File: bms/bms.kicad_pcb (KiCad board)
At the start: 2 copper layers, 89.7 x 150.1 mm, 27 parts, among them J1 Conn_01x16_Pin, J10 Conn_01x02_Pin, J11 Conn_01x02_Pin, J12 Conn_01x02_Pin, J13 Conn_01x02_Pin, J14 Conn_01x08_Pin, J15 Conn_01x08_Pin, J16 Conn_01x02_Pin, J17 Conn_01x08_Pin, J18 Conn_01x08_Pin, J19 Conn_01x08_Pin, J2 Conn_01x16_Pin, J20 Conn_01x08_Pin, J21 Conn_01x08_Pin, J22 Conn_01x08_Socket, J23 Conn_01x10_Socket, J24 Conn_01x08_Pin, J25 Conn_01x02_Pin, J26 Conn_01x06_Socket, J27 Conn_01x06_Socket, J3 Conn_01x02_Pin, J4 Conn_01x02_Pin, J5 Conn_01x02_Pin, J6 Conn_01x16_Pin, J7 Conn_01x20_Pin, J8 Conn_01x20_Pin, J9 Conn_01x02_Pin

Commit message: prajeala_maxima_3
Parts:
- removed the J1 at (114.6, 74.7)
- removed the J2 at (114.6, 51.8)
- removed the J6 at (162.8, 87.4)
- removed the J7 at (114.6, 97.5)
- removed the J8 at (162.8, 115.3)
- added J10: Conn_02x08_Odd_Even, Connector_PinHeader_2.54mm:PinHeader_2x08_P2.54mm_Vertical, B.Cu at (279.6, 123.8)
- added J11: Conn_02x10_Odd_Even, Connector_PinHeader_2.54mm:PinHeader_2x10_P2.54mm_Vertical, B.Cu at (279.7, 151.7)
- added J20: Conn_02x08_Odd_Even, Connector_PinHeader_2.54mm:PinHeader_2x08_P2.54mm_Vertical, B.Cu at (231.4, 88.2)
- added J21: Conn_02x08_Odd_Even, Connector_PinHeader_2.54mm:PinHeader_2x08_P2.54mm_Vertical, B.Cu at (231.4, 111.1)
- added J22: Conn_02x10_Odd_Even, Connector_PinHeader_2.54mm:PinHeader_2x10_P2.54mm_Vertical, B.Cu at (231.4, 133.9)
- moved J7 98.1 mm to (220.6, 43.6)
- moved J12 98.1 mm to (245.6, 43.6)
- moved J13 98.1 mm to (253.9, 43.6)
- moved J23 98.1 mm to (262.3, 43.6)
- moved J8 98.1 mm to (228.9, 43.6)
- moved J9 98.1 mm to (237.2, 43.6)
- moved J4 98.1 mm to (212.2, 43.6)
- moved J1 98.1 mm to (270.6, 43.6)
- moved J25 65.0 mm to (50.8, 148.8)
- moved J24 65.0 mm to (50.8, 157.9)
- moved J2 64.7 mm to (155.0, 109.3)
- moved J3 64.7 mm to (155.0, 132.1)
- moved J5 64.7 mm to (202.9, 105.5)
- moved J6 64.7 mm to (202.9, 132.1)
- moved J27 63.8 mm to (87.3, 153.0)
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- renumbered J24 to J1, J19 to J12, J20 to J13, J11 to J14, J13 to J15, J4 to J17, J9 to J18, J10 to J19, J22 to J2, J21 to J23, J3 to J24, J5 to J25, J25 to J26, J12 to J27, J27 to J3, J14 to J4, J23 to J5, J26 to J6, J15 to J7, J17 to J8, J18 to J9
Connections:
- J26 pad 1: Net-(J23-Pin_10) -> GND
- J26 pad 2: Net-(J2-Pin_16) -> Vout+
- J5 pad 10: Net-(J23-Pin_10) -> unconnected-(J5-Pin_10-Pad10)
- J5 pad 2: unconnected-(J23-Pin_2-Pad2) -> cs
- J5 pad 3: unconnected-(J23-Pin_3-Pad3) -> sout
- J5 pad 4: cs -> miso
- J5 pad 5: sout -> sck
- J5 pad 6: miso -> Vdd
- J5 pad 7: sck -> unconnected-(J5-Pin_7-Pad7)
- J5 pad 8: Vdd -> GND
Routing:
- net Net-(J2-Pin_16): track 93.8 -> 0.00 mm
- net sout: track 83.3 -> 0.00 mm
- net Net-(J16-Pin_2): track 74.9 -> 0.00 mm
- net Vdd: track 72.2 -> 0.00 mm
- net 8: track 129.7 -> 58.4 mm
- net Net-(J15-Pin_2): track 69.8 -> 0.00 mm
- net Net-(J15-Pin_1): track 69.7 -> 0.00 mm
- net Net-(J16-Pin_1): track 69.2 -> 0.00 mm
- net Net-(J23-Pin_10): track 68.0 -> 0.00 mm
- net Net-(J14-Pin_1): track 65.6 -> 0.00 mm
- net 7: track 123.5 -> 58.4 mm
- net Net-(J14-Pin_2): track 64.5 -> 0.00 mm
- net 6: track 118.2 -> 58.4 mm
- net Net-(J17-Pin_2): track 56.6 -> 0.00 mm
- net 5: track 112.8 -> 58.4 mm
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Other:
- board outline removed

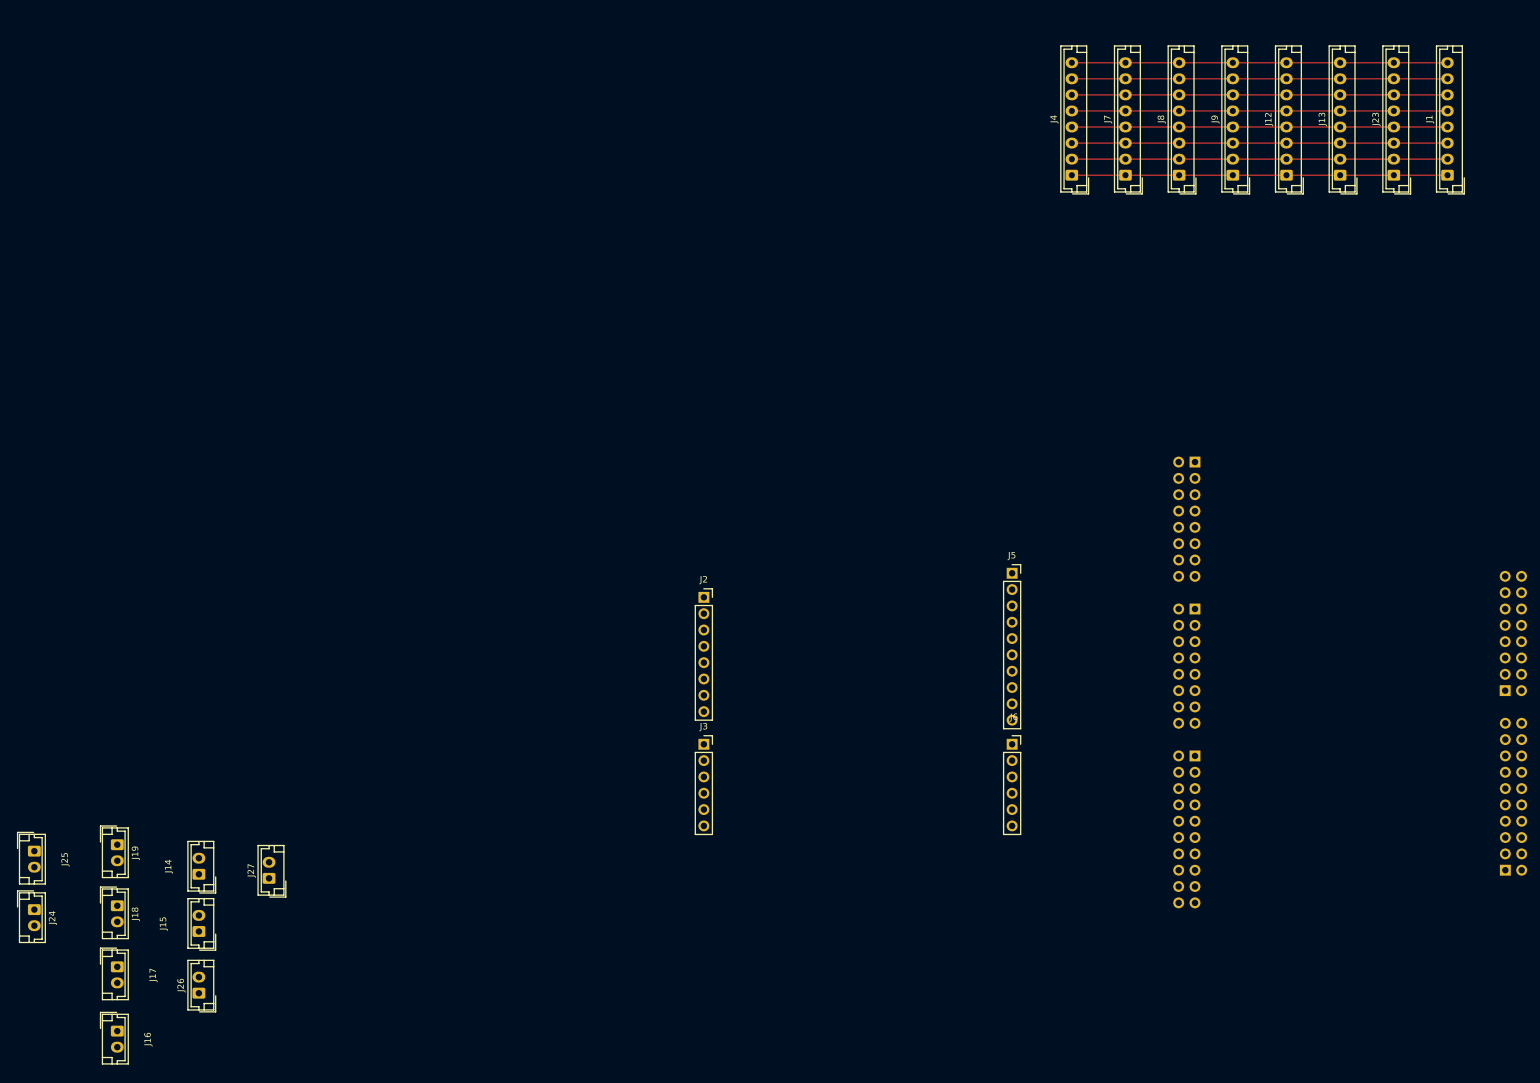
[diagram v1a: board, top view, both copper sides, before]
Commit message: idee de pcb bms
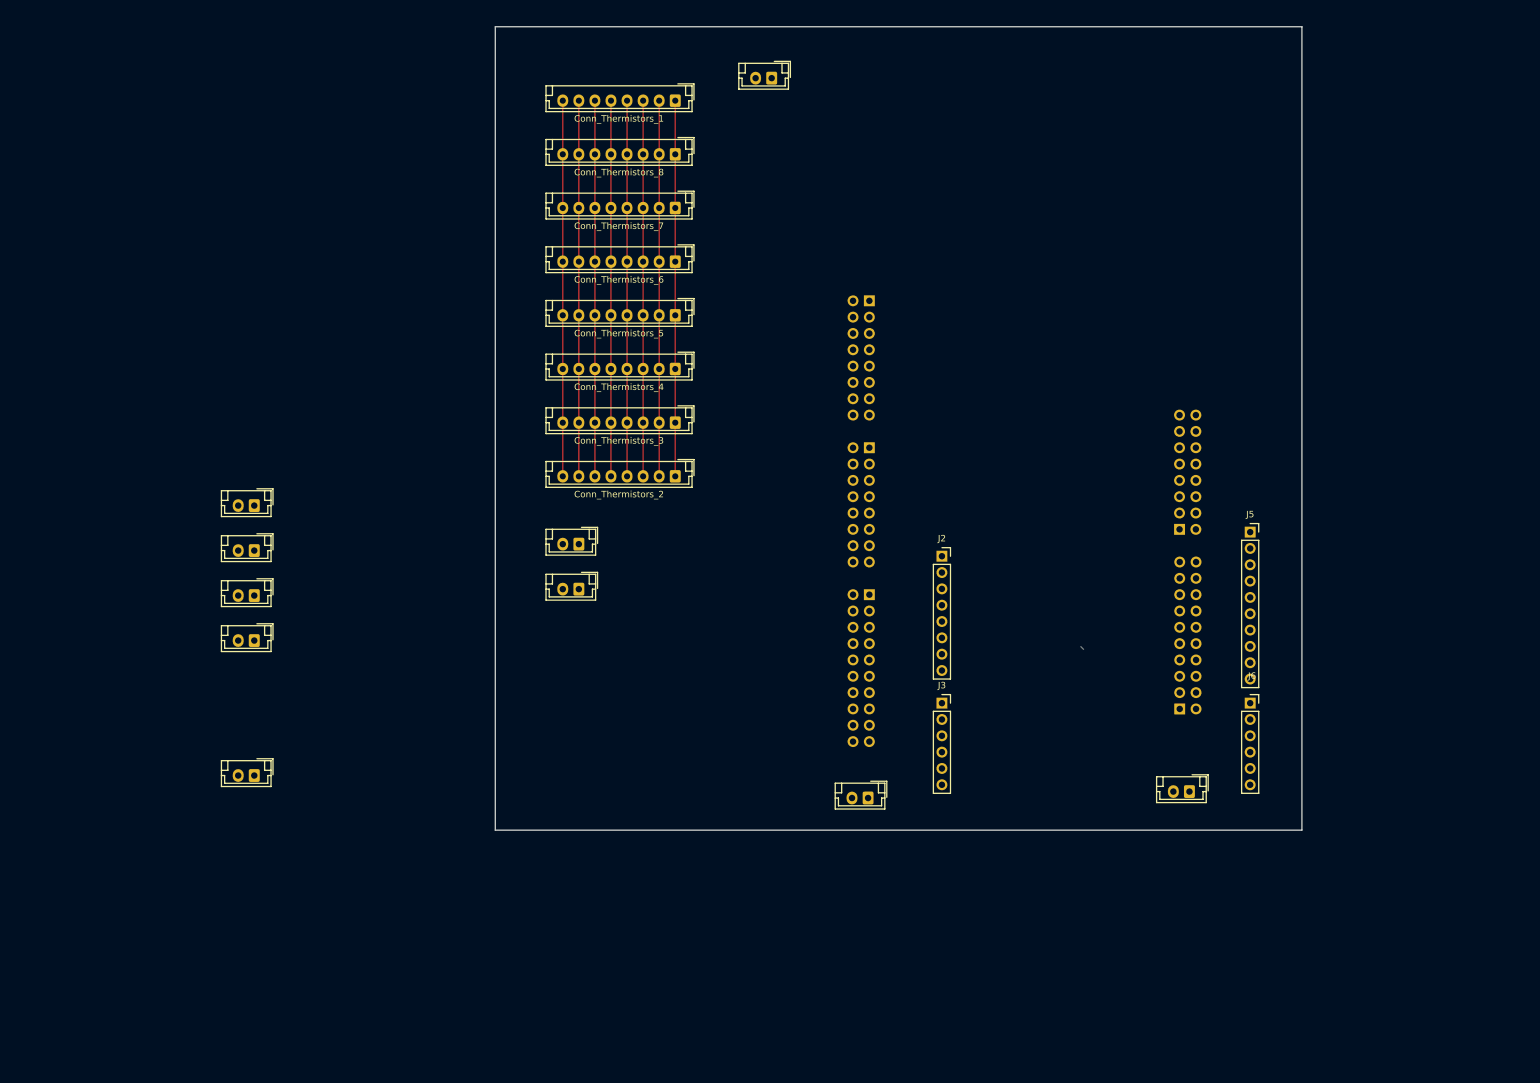
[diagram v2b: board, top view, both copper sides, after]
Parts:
- moved Soft_G_B5-6 179.9 mm to (165.5, 28.5), turned to 180 degrees
- moved Vdd1 143.8 mm to (230.5, 139.5), turned to 180 degrees
- moved Conn_Thermistors_1 120.7 mm to (150.5, 32.0), turned to 180 degrees
- moved Conn_Thermistors_8 111.8 mm to (150.5, 40.4), turned to 180 degrees
- moved Battery1 108.5 mm to (180.5, 140.5), turned to 180 degrees
- moved Conn_Thermistors_7 103.6 mm to (150.5, 48.7), turned to 180 degrees
- moved Conn_Thermistors_6 96.0 mm to (150.5, 57.0), turned to 180 degrees
- moved Conn_Thermistors_5 89.4 mm to (150.5, 65.4), turned to 180 degrees
- moved Soft_G_B1-2 84.4 mm to (135.5, 101.0), turned to 180 degrees
- moved Conn_Thermistors_4 84.0 mm to (150.5, 73.8), turned to 180 degrees
- moved Conn_Thermistors_3 79.9 mm to (150.5, 82.1), turned to 180 degrees
- moved Conn_Thermistors_2 77.5 mm to (150.5, 90.5), turned to 180 degrees
- moved Soft_G_B3-4 73.9 mm to (135.5, 108.0), turned to 180 degrees
- moved Soft_G_B15-16 68.2 mm to (85.0, 102.0), turned to 180 degrees
- moved Soft_G_B7-8 63.7 mm to (85.0, 95.0), turned to 180 degrees
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- renumbered J26 to Battery1, J1 to Conn_Thermistors_1, J4 to Conn_Thermistors_2, J7 to Conn_Thermistors_3, J8 to Conn_Thermistors_4, J9 to Conn_Thermistors_5, J12 to Conn_Thermistors_6, J13 to Conn_Thermistors_7, J23 to Conn_Thermistors_8, J20 to J13, J21 to J14, J15 to Soft_G_B1-2, J19 to Soft_G_B11-12, J18 to Soft_G_B13-14, J17 to Soft_G_B15-16, J14 to Soft_G_B3-4, J16 to Soft_G_B5-6, J25 to Soft_G_B7-8, J24 to Soft_G_B9-10, J27 to Vdd1
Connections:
- Battery1 pad 2: Vout+ -> Bat+
- J11 pad 10: GND -> unconnected-(J11-Pin_10-Pad10)
- J11 pad 12: Vdd -> unconnected-(J11-Pin_12-Pad12)
- J11 pad 17: sout -> unconnected-(J11-Pin_17-Pad17)
- J11 pad 18: cs -> unconnected-(J11-Pin_18-Pad18)
- J11 pad 19: sck -> unconnected-(J11-Pin_19-Pad19)
- J11 pad 20: miso -> unconnected-(J11-Pin_20-Pad20)
- J13 pad 16: Vout+ -> unconnected-(J13-Pin_16-Pad16)
- J14 pad 10: 5 -> unconnected-(J14-Pin_10-Pad10)
- J14 pad 11: Net-(J15-Pin_2) -> unconnected-(J14-Pin_11-Pad11)
- J14 pad 12: 6 -> unconnected-(J14-Pin_12-Pad12)
- J14 pad 14: 7 -> unconnected-(J14-Pin_14-Pad14)
- J14 pad 16: 8 -> unconnected-(J14-Pin_16-Pad16)
- J14 pad 2: 1 -> unconnected-(J14-Pin_2-Pad2)
- J14 pad 4: 2 -> unconnected-(J14-Pin_4-Pad4)
- J14 pad 5: Net-(J14-Pin_1) -> unconnected-(J14-Pin_5-Pad5)
- J14 pad 6: 3 -> unconnected-(J14-Pin_6-Pad6)
- J14 pad 7: Net-(J14-Pin_2) -> unconnected-(J14-Pin_7-Pad7)
- J14 pad 8: 4 -> unconnected-(J14-Pin_8-Pad8)
- J14 pad 9: Net-(J15-Pin_1) -> unconnected-(J14-Pin_9-Pad9)
- J22 pad 1: Net-(J16-Pin_1) -> unconnected-(J22-Pin_1-Pad1)
- J22 pad 10: Net-(J22-Pin_10) -> unconnected-(J22-Pin_10-Pad10)
- J22 pad 12: Net-(J22-Pin_12) -> unconnected-(J22-Pin_12-Pad12)
- J22 pad 13: Net-(J18-Pin_1) -> unconnected-(J22-Pin_13-Pad13)
- J22 pad 15: Net-(J18-Pin_2) -> unconnected-(J22-Pin_15-Pad15)
- J22 pad 17: Net-(J19-Pin_1) -> unconnected-(J22-Pin_17-Pad17)
- J22 pad 19: Net-(J19-Pin_2) -> unconnected-(J22-Pin_19-Pad19)
- J22 pad 2: Net-(J22-Pin_2) -> unconnected-(J22-Pin_2-Pad2)
- J22 pad 3: Net-(J16-Pin_2) -> unconnected-(J22-Pin_3-Pad3)
- J22 pad 4: Net-(J22-Pin_4) -> unconnected-(J22-Pin_4-Pad4)
- J22 pad 5: Net-(J17-Pin_1) -> unconnected-(J22-Pin_5-Pad5)
- J22 pad 7: Net-(J17-Pin_2) -> unconnected-(J22-Pin_7-Pad7)
- J5 pad 2: cs -> CS
- J5 pad 3: sout -> SOUT
- J5 pad 4: miso -> MISO
- J5 pad 5: sck -> SCK
- Soft_G_B1-2 pad 1: Net-(J15-Pin_1) -> G2
- Soft_G_B1-2 pad 2: Net-(J15-Pin_2) -> G1
- Soft_G_B11-12 pad 1: Net-(J19-Pin_1) -> G12
- Soft_G_B11-12 pad 2: Net-(J19-Pin_2) -> G11
- Soft_G_B13-14 pad 1: Net-(J18-Pin_1) -> G14
- Soft_G_B13-14 pad 2: Net-(J18-Pin_2) -> G13
- Soft_G_B15-16 pad 1: Net-(J17-Pin_1) -> G16
- Soft_G_B15-16 pad 2: Net-(J17-Pin_2) -> G15
- Soft_G_B3-4 pad 1: Net-(J14-Pin_1) -> G4
- Soft_G_B3-4 pad 2: Net-(J14-Pin_2) -> G3
- Soft_G_B5-6 pad 1: Net-(J16-Pin_1) -> G6
- Soft_G_B5-6 pad 2: Net-(J16-Pin_2) -> G5
- Soft_G_B7-8 pad 1: Net-(J22-Pin_12) -> G8
- Soft_G_B7-8 pad 2: Net-(J22-Pin_10) -> G7
- Soft_G_B9-10 pad 1: Net-(J22-Pin_4) -> G10
- Soft_G_B9-10 pad 2: Net-(J22-Pin_2) -> G9
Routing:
- net unconnected-(J11-Pin_10-Pad10): track 0.00 -> 0.61 mm
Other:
- board outline added: 125.5 x 125 mm

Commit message: fara program deschis
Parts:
- moved Soft_G_B5-6 73.7 mm to (152.5, 101.0)
- moved Soft_G_B15-16 72.3 mm to (152.5, 128.0)
- moved Soft_G_B13-14 69.4 mm to (152.5, 121.0)
- moved Soft_G_B7-8 68.7 mm to (152.5, 108.0)
- moved Soft_G_B11-12 47.9 mm to (129.0, 128.0)
- moved Soft_G_B9-10 44.3 mm to (129.0, 121.0)
- moved Soft_G_B1-2 6.50 mm to (129.0, 101.0)
- moved Soft_G_B3-4 6.50 mm to (129.0, 108.0)
- moved Conn_Thermistors_2 1.66 mm to (149.0, 89.8)
- moved Conn_Thermistors_4 1.66 mm to (149.0, 73.0)
- moved Conn_Thermistors_5 1.66 mm to (149.0, 64.7)
- moved Conn_Thermistors_7 1.66 mm to (149.0, 48.0)
- moved Conn_Thermistors_8 1.66 mm to (149.0, 39.6)
- moved Conn_Thermistors_1 1.66 mm to (149.0, 31.3)
- moved Conn_Thermistors_6 1.66 mm to (149.0, 56.4)
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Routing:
- net unconnected-(J11-Pin_10-Pad10): track 0.61 -> 0.00 mm
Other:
- board size 125.5 x 125 mm -> 134 x 125 mm
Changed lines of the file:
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@@
 	(footprint "Connector_JST:JST_EH_B8B-EH-A_1x08_P2.50mm_Vertical"
 		(layer "F.Cu")
-		(at 150.5 82.1 180)
+		(at 149 81.4 180)
 		(descr "JST EH series connector, B8B-EH-A (http://www.jst-mfg.com/product/pdf/eng/eEH.pdf), generated with kicad-footprint-generator")
 		(tags "connector JST EH vertical")
@@
 	(footprint "Connector_JST:JST_EH_B8B-EH-A_1x08_P2.50mm_Vertical"
 		(layer "F.Cu")
-		(at 150.5 57.05 180)
+		(at 149 56.35 180)
 		(descr "JST EH series connector, B8B-EH-A (http://www.jst-mfg.com/product/pdf/eng/eEH.pdf), generated with kicad-footprint-generator")
 		(tags "connector JST EH vertical")
@@
 	(footprint "Connector_JST:JST_EH_B2B-EH-A_1x02_P2.50mm_Vertical"
 		(layer "F.Cu")
-		(at 135.5 108 180)
+		(at 129 108 180)
 		(descr "JST EH series connector, B2B-EH-A (http://www.jst-mfg.com/product/pdf/eng/eEH.pdf), generated with kicad-footprint-generator")
 		(tags "connector JST EH vertical")
@@
 		)
 		(fp_text user "${REFERENCE}"
-			(at 1.25 1.5 0)
+			(at -8.5 0.5 0)
 			(layer "F.Fab")
 			(effects
@@
 	(footprint "Connector_JST:JST_EH_B2B-EH-A_1x02_P2.50mm_Vertical"
 		(layer "F.Cu")
-		(at 85 137 180)
+		(at 152.5 121 180)
 		(descr "JST EH series connector, B2B-EH-A (http://www.jst-mfg.com/product/pdf/eng/eEH.pdf), generated with kicad-footprint-generator")
 		(tags "connector JST EH vertical")
@@
 		)
 		(fp_text user "${REFERENCE}"
-			(at 1.25 1.5 0)
+			(at -9.5 0 0)
 			(layer "F.Fab")
 			(effects
@@
 	(footprint "Connector_JST:JST_EH_B2B-EH-A_1x02_P2.50mm_Vertical"
 		(layer "F.Cu")
-		(at 85 102 180)
+		(at 152.5 128 180)
 		(descr "JST EH series connector, B2B-EH-A (http://www.jst-mfg.com/product/pdf/eng/eEH.pdf), generated with kicad-footprint-generator")
 		(tags "connector JST EH vertical")
@@
 		)
 		(fp_text user "${REFERENCE}"
-			(at 1.25 1.5 0)
+			(at -9.5 0 0)
 			(layer "F.Fab")
 			(effects
@@
 	(footprint "Connector_JST:JST_EH_B8B-EH-A_1x08_P2.50mm_Vertical"
 		(layer "F.Cu")
-		(at 150.5 73.75 180)
+		(at 149 73.05 180)
 		(descr "JST EH series connector, B8B-EH-A (http://www.jst-mfg.com/product/pdf/eng/eEH.pdf), generated with kicad-footprint-generator")
 		(tags "connector JST EH vertical")
@@
 	(footprint "Connector_JST:JST_EH_B2B-EH-A_1x02_P2.50mm_Vertical"
 		(layer "F.Cu")
-		(at 135.5 101 180)
+		(at 129 101 180)
 		(descr "JST EH series connector, B2B-EH-A (http://www.jst-mfg.com/product/pdf/eng/eEH.pdf), generated with kicad-footprint-generator")
 		(tags "connector JST EH vertical")
@@
 		)
 		(fp_text user "${REFERENCE}"
-			(at 1.25 1.5 0)
+			(at -8.5 0 0)
 			(layer "F.Fab")
 			(effects
@@
 	(footprint "Connector_JST:JST_EH_B8B-EH-A_1x08_P2.50mm_Vertical"
 		(layer "F.Cu")
-		(at 150.5 65.4 180)
+		(at 149 64.7 180)
 		(descr "JST EH series connector, B8B-EH-A (http://www.jst-mfg.com/product/pdf/eng/eEH.pdf), generated with kicad-footprint-generator")
 		(tags "connector JST EH vertical")
@@
 	(footprint "Connector_JST:JST_EH_B8B-EH-A_1x08_P2.50mm_Vertical"
 		(layer "F.Cu")
-		(at 150.5 48.7 180)
+		(at 149 48 180)
 		(descr "JST EH series connector, B8B-EH-A (http://www.jst-mfg.com/product/pdf/eng/eEH.pdf), generated with kicad-footprint-generator")
 		(tags "connector JST EH vertical")
@@
 	(footprint "Connector_JST:JST_EH_B8B-EH-A_1x08_P2.50mm_Vertical"
 		(layer "F.Cu")
-		(at 150.5 90.45 180)
+		(at 149 89.75 180)
 		(descr "JST EH series connector, B8B-EH-A (http://www.jst-mfg.com/product/pdf/eng/eEH.pdf), generated with kicad-footprint-generator")
 		(tags "connector JST EH vertical")
@@
 	(footprint "Connector_JST:JST_EH_B2B-EH-A_1x02_P2.50mm_Vertical"
 		(layer "F.Cu")
-		(at 85 109 180)
+		(at 129 128 180)
 		(descr "JST EH series connector, B2B-EH-A (http://www.jst-mfg.com/product/pdf/eng/eEH.pdf), generated with kicad-footprint-generator")
 		(tags "connector JST EH vertical")
@@
 		)
 		(fp_text user "${REFERENCE}"
-			(at 1.25 1.5 0)
+			(at -9.5 0 0)
 			(layer "F.Fab")
 			(effects
@@
 	(footprint "Connector_JST:JST_EH_B2B-EH-A_1x02_P2.50mm_Vertical"
 		(layer "F.Cu")
-		(at 85 116 180)
+		(at 129 121 180)
 		(descr "JST EH series connector, B2B-EH-A (http://www.jst-mfg.com/product/pdf/eng/eEH.pdf), generated with kicad-footprint-generator")
 		(tags "connector JST EH vertical")
@@
 		)
 		(fp_text user "${REFERENCE}"
-			(at 1.25 3.8 0)
+			(at -9 0 0)
 			(layer "F.Fab")
 			(effects
@@
 	(footprint "Connector_JST:JST_EH_B2B-EH-A_1x02_P2.50mm_Vertical"
 		(layer "F.Cu")
-		(at 230.5 139.5 180)
+		(at 231.75 140.5 180)
 		(descr "JST EH series connector, B2B-EH-A (http://www.jst-mfg.com/product/pdf/eng/eEH.pdf), generated with kicad-footprint-generator")
 		(tags "connector JST EH vertical")
@@
 	(footprint "Connector_JST:JST_EH_B2B-EH-A_1x02_P2.50mm_Vertical"
 		(layer "F.Cu")
-		(at 85 95 180)
+		(at 152.5 108 180)
 		(descr "JST EH series connector, B2B-EH-A (http://www.jst-mfg.com/product/pdf/eng/eEH.pdf), generated with kicad-footprint-generator")
 		(tags "connector JST EH vertical")
@@
 		)
 		(fp_text user "${REFERENCE}"
-			(at 1.25 3.8 0)
+			(at -8.5 0 0)
 			(layer "F.Fab")
 			(effects
@@
 	(footprint "Connector_JST:JST_EH_B8B-EH-A_1x08_P2.50mm_Vertical"
 		(layer "F.Cu")
-		(at 150.5 32 180)
+		(at 149 31.3 180)
 		(descr "JST EH series connector, B8B-EH-A (http://www.jst-mfg.com/product/pdf/eng/eEH.pdf), generated with kicad-footprint-generator")
 		(tags "connector JST EH vertical")
@@
 	(footprint "Connector_JST:JST_EH_B2B-EH-A_1x02_P2.50mm_Vertical"
 		(layer "F.Cu")
-		(at 165.5 28.5 180)
+		(at 152.5 101 180)
 		(descr "JST EH series connector, B2B-EH-A (http://www.jst-mfg.com/product/pdf/eng/eEH.pdf), generated with kicad-footprint-generator")
 		(tags "connector JST EH vertical")
@@
 		)
 		(fp_text user "${REFERENCE}"
-			(at 1.25 1.5 0)
+			(at -8.5 0 0)
 			(layer "F.Fab")
 			(effects
@@
 	(footprint "Connector_JST:JST_EH_B8B-EH-A_1x08_P2.50mm_Vertical"
 		(layer "F.Cu")
-		(at 150.5 40.35 180)
+		(at 149 39.65 180)
 		(descr "JST EH series connector, B8B-EH-A (http://www.jst-mfg.com/product/pdf/eng/eEH.pdf), generated with kicad-footprint-generator")
 		(tags "connector JST EH vertical")
@@
 	)
 	(gr_rect
-		(start 122.5 20.5)
+		(start 114 20.5)
 		(end 248 145.5)
 		(stroke
@@
 	)
 	(segment
-		(start 138 32)
-		(end 138 90.45)
+		(start 136.5 31.3)
+		(end 136.5 89.75)
 		(width 0.2)
 		(layer "F.Cu")
@@
 	)
 	(segment
-		(start 150.5 32)
-		(end 150.5 40.35)
+		(start 149 31.3)
+		(end 149 39.65)
 		(width 0.2)
 		(layer "F.Cu")
@@
 	)
 	(segment
-		(start 150.5 57.05)
-		(end 150.5 90.45)
+		(start 149 56.35)
+		(end 149 89.75)
 		(width 0.2)
 		(layer "F.Cu")
@@
 	)
 	(segment
-		(start 150.5 48.7)
-		(end 150.5 57.05)
+		(start 149 48)
+		(end 149 56.35)
 		(width 0.2)
 		(layer "F.Cu")
@@
 	)
 	(segment
-		(start 150.5 40.35)
-		(end 150.5 48.7)
+		(start 149 39.65)
+		(end 149 48)
 		(width 0.2)
 		(layer "F.Cu")
@@
 	)
 	(segment
-		(start 148 32)
-		(end 148 90.45)
+		(start 146.5 31.3)
+		(end 146.5 89.75)
 		(width 0.2)
 		(layer "F.Cu")
@@
 	)
 	(segment
-		(start 145.5 90.45)
-		(end 145.5 32)
+		(start 144 89.75)
+		(end 144 31.3)
 		(width 0.2)
 		(layer "F.Cu")
@@
 	)
 	(segment
-		(start 140.5 90.45)
-		(end 140.5 32)
+		(start 139 89.75)
+		(end 139 31.3)
 		(width 0.2)
 		(layer "F.Cu")
@@
 	)
 	(segment
-		(start 143 32)
-		(end 143 90.45)
+		(start 141.5 31.3)
+		(end 141.5 89.75)
 		(width 0.2)
 		(layer "F.Cu")
@@
 	)
 	(segment
-		(start 135.5 32)
-		(end 135.5 90.45)
+		(start 134 31.3)
+		(end 134 89.75)
 		(width 0.2)
 		(layer "F.Cu")
@@
 	)
 	(segment
-		(start 133 32)
-		(end 133 90.45)
+		(start 131.5 31.3)
+		(end 131.5 89.75)
 		(width 0.2)
 		(layer "F.Cu")
 		(net 26)
 	)
-	(segment
-		(start 214.0313 117.38)
-		(end 213.6013 116.95)
-		(width 0.2)
-		(layer "B.Cu")
-		(net 109)
-	)
 	(group ""
